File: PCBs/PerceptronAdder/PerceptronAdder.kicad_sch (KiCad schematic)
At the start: 80 parts, among them J1 Conn_02x10, J2 Conn_01x02_Pin, J3 Conn_01x02_Socket, K1 6mm, K10 6mm, K11 6mm, K12 6mm, K13 6mm, K14 6mm, K15 6mm, K16 6mm, K17 6mm, K2 6mm, K3 6mm, K4 6mm, K5 6mm, K6 6mm, K7 6mm, K8 6mm, K9 6mm

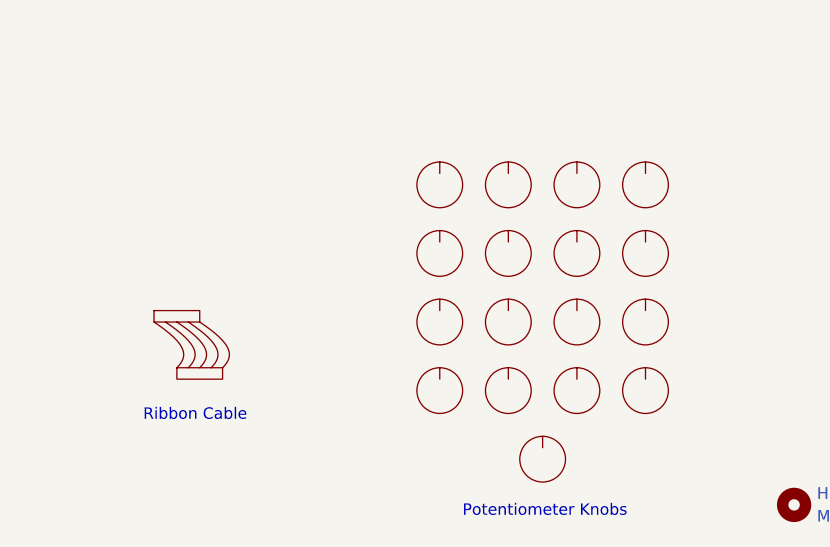
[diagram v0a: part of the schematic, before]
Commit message: Remove knobs from BoM and add alternate link for ribbon cable.
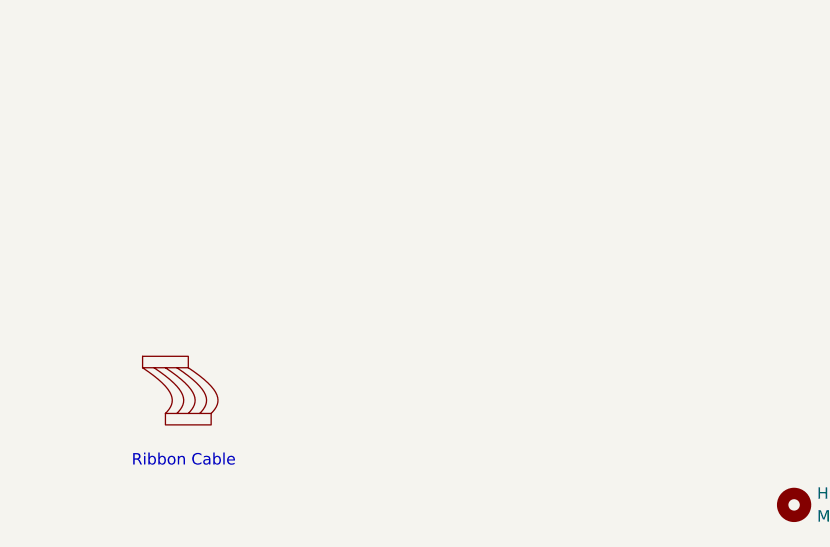
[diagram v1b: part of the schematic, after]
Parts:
- removed K1, K10, K11, K12, K13, K14, K15, K16, K17, K2, K3, K4, K5, K6, K7, K8, K9: 6mm, symbol PerceptronAdderSymbols:Potentiometer_Knob
- RC1: Alt Link (none) -> https://www.digikey.com/en/products/detail/assmann-wsw-comp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
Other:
- note removed: "Potentiometer Knobs"

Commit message: Added resistor values to silkscreen.
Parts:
- R1, R10, R11, R12, R13, R14, R15, R16, R17, R18, R19, R2, R20, R21, R22, R23, R24, R25, R26, R27, R28, R29, R3, R30, R31, R32, R33, R34, R35, R36, R37, R4, R5, R6, R7, R8, R9: footprint Resistor_THT:R_Axial_DIN0207_L6.3mm_D2.5mm_P7.62mm_Horizontal -> PerceptronAdderFootprints:R_Axial_DIN0207_L6.3mm_D2.5mm_P7.62mm_Horizontal
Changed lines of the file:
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@@
 	(title_block
 		(title "Perceptron Adder")
-		(date "2026-03-11")
-		(rev "2.2")
+		(date "2026-05-21")
+		(rev "2.3")
 		(company "RDB64")
 	)
@@
 			)
 		)
-		(property "Footprint" "Resistor_THT:R_Axial_DIN0207_L6.3mm_D2.5mm_P7.62mm_Horizontal"
+		(property "Footprint" "PerceptronAdderFootprints:R_Axial_DIN0207_L6.3mm_D2.5mm_P7.62mm_Horizontal"
 			(at 206.502 83.82 90)
 			(effects
@@
 			)
 		)
-		(property "Footprint" "Resistor_THT:R_Axial_DIN0207_L6.3mm_D2.5mm_P7.62mm_Horizontal"
+		(property "Footprint" "PerceptronAdderFootprints:R_Axial_DIN0207_L6.3mm_D2.5mm_P7.62mm_Horizontal"
 			(at 51.562 83.82 90)
 			(effects
@@
 			)
 		)
-		(property "Footprint" "Resistor_THT:R_Axial_DIN0207_L6.3mm_D2.5mm_P7.62mm_Horizontal"
+		(property "Footprint" "PerceptronAdderFootprints:R_Axial_DIN0207_L6.3mm_D2.5mm_P7.62mm_Horizontal"
 			(at 89.662 83.82 90)
 			(effects
@@
 			)
 		)
-		(property "Footprint" "Resistor_THT:R_Axial_DIN0207_L6.3mm_D2.5mm_P7.62mm_Horizontal"
+		(property "Footprint" "PerceptronAdderFootprints:R_Axial_DIN0207_L6.3mm_D2.5mm_P7.62mm_Horizontal"
 			(at 229.362 83.82 90)
 			(effects
@@
 			)
 		)
-		(property "Footprint" "Resistor_THT:R_Axial_DIN0207_L6.3mm_D2.5mm_P7.62mm_Horizontal"
+		(property "Footprint" "PerceptronAdderFootprints:R_Axial_DIN0207_L6.3mm_D2.5mm_P7.62mm_Horizontal"
 			(at 36.322 83.82 90)
 			(effects
@@
 			)
 		)
-		(property "Footprint" "Resistor_THT:R_Axial_DIN0207_L6.3mm_D2.5mm_P7.62mm_Horizontal"
+		(property "Footprint" "PerceptronAdderFootprints:R_Axial_DIN0207_L6.3mm_D2.5mm_P7.62mm_Horizontal"
 			(at 244.602 83.82 90)
 			(effects
@@
 			)
 		)
-		(property "Footprint" "Resistor_THT:R_Axial_DIN0207_L6.3mm_D2.5mm_P7.62mm_Horizontal"
+		(property "Footprint" "PerceptronAdderFootprints:R_Axial_DIN0207_L6.3mm_D2.5mm_P7.62mm_Horizontal"
 			(at 198.882 83.82 90)
 			(effects
@@
 			)
 		)
-		(property "Footprint" "Resistor_THT:R_Axial_DIN0207_L6.3mm_D2.5mm_P7.62mm_Horizontal"
+		(property "Footprint" "PerceptronAdderFootprints:R_Axial_DIN0207_L6.3mm_D2.5mm_P7.62mm_Horizontal"
 			(at 13.462 83.82 90)
 			(effects
@@
 			)
 		)
-		(property "Footprint" "Resistor_THT:R_Axial_DIN0207_L6.3mm_D2.5mm_P7.62mm_Horizontal"
+		(property "Footprint" "PerceptronAdderFootprints:R_Axial_DIN0207_L6.3mm_D2.5mm_P7.62mm_Horizontal"
 			(at 43.942 83.82 90)
 			(effects
@@
 			)
 		)
-		(property "Footprint" "Resistor_THT:R_Axial_DIN0207_L6.3mm_D2.5mm_P7.62mm_Horizontal"
+		(property "Footprint" "PerceptronAdderFootprints:R_Axial_DIN0207_L6.3mm_D2.5mm_P7.62mm_Horizontal"
 			(at 262.382 83.82 90)
 			(effects
@@
 			)
 		)
-		(property "Footprint" "Resistor_THT:R_Axial_DIN0207_L6.3mm_D2.5mm_P7.62mm_Horizontal"
+		(property "Footprint" "PerceptronAdderFootprints:R_Axial_DIN0207_L6.3mm_D2.5mm_P7.62mm_Horizontal"
 			(at 21.082 83.82 90)
 			(effects
@@
 			)
 		)
-		(property "Footprint" "Resistor_THT:R_Axial_DIN0207_L6.3mm_D2.5mm_P7.62mm_Horizontal"
+		(property "Footprint" "PerceptronAdderFootprints:R_Axial_DIN0207_L6.3mm_D2.5mm_P7.62mm_Horizontal"
 			(at 74.422 83.82 90)
 			(effects
@@
 			)
 		)
-		(property "Footprint" "Resistor_THT:R_Axial_DIN0207_L6.3mm_D2.5mm_P7.62mm_Horizontal"
+		(property "Footprint" "PerceptronAdderFootprints:R_Axial_DIN0207_L6.3mm_D2.5mm_P7.62mm_Horizontal"
 			(at 97.282 83.82 90)
 			(effects
@@
 			)
 		)
-		(property "Footprint" "Resistor_THT:R_Axial_DIN0207_L6.3mm_D2.5mm_P7.62mm_Horizontal"
+		(property "Footprint" "PerceptronAdderFootprints:R_Axial_DIN0207_L6.3mm_D2.5mm_P7.62mm_Horizontal"
 			(at 160.782 83.82 90)
 			(effects
@@
 			)
 		)
-		(property "Footprint" "Resistor_THT:R_Axial_DIN0207_L6.3mm_D2.5mm_P7.62mm_Horizontal"
+		(property "Footprint" "PerceptronAdderFootprints:R_Axial_DIN0207_L6.3mm_D2.5mm_P7.62mm_Horizontal"
 			(at 28.702 83.82 90)
 			(effects
@@
 			)
 		)
-		(property "Footprint" "Resistor_THT:R_Axial_DIN0207_L6.3mm_D2.5mm_P7.62mm_Horizontal"
+		(property "Footprint" "PerceptronAdderFootprints:R_Axial_DIN0207_L6.3mm_D2.5mm_P7.62mm_Horizontal"
 			(at 191.262 83.82 90)
 			(effects
@@
 			)
 		)
-		(property "Footprint" "Resistor_THT:R_Axial_DIN0207_L6.3mm_D2.5mm_P7.62mm_Horizontal"
+		(property "Footprint" "PerceptronAdderFootprints:R_Axial_DIN0207_L6.3mm_D2.5mm_P7.62mm_Horizontal"
 			(at 259.842 114.3 90)
 			(effects
@@
 			)
 		)
-		(property "Footprint" "Resistor_THT:R_Axial_DIN0207_L6.3mm_D2.5mm_P7.62mm_Horizontal"
+		(property "Footprint" "PerceptronAdderFootprints:R_Axial_DIN0207_L6.3mm_D2.5mm_P7.62mm_Horizontal"
 			(at 214.122 83.82 90)
 			(effects
@@
 			)
 		)
-		(property "Footprint" "Resistor_THT:R_Axial_DIN0207_L6.3mm_D2.5mm_P7.62mm_Horizontal"
+		(property "Footprint" "PerceptronAdderFootprints:R_Axial_DIN0207_L6.3mm_D2.5mm_P7.62mm_Horizontal"
 			(at 112.522 83.82 90)
 			(effects
@@
 			)
 		)
-		(property "Footprint" "Resistor_THT:R_Axial_DIN0207_L6.3mm_D2.5mm_P7.62mm_Horizontal"
+		(property "Footprint" "PerceptronAdderFootprints:R_Axial_DIN0207_L6.3mm_D2.5mm_P7.62mm_Horizontal"
 			(at 127.762 83.82 90)
 			(effects
@@
 			)
 		)
-		(property "Footprint" "Resistor_THT:R_Axial_DIN0207_L6.3mm_D2.5mm_P7.62mm_Horizontal"
+		(property "Footprint" "PerceptronAdderFootprints:R_Axial_DIN0207_L6.3mm_D2.5mm_P7.62mm_Horizontal"
 			(at 59.182 83.82 90)
 			(effects
@@
 			)
 		)
-		(property "Footprint" "Resistor_THT:R_Axial_DIN0207_L6.3mm_D2.5mm_P7.62mm_Horizontal"
+		(property "Footprint" "PerceptronAdderFootprints:R_Axial_DIN0207_L6.3mm_D2.5mm_P7.62mm_Horizontal"
 			(at 183.642 83.82 90)
 			(effects
@@
 			)
 		)
-		(property "Footprint" "Resistor_THT:R_Axial_DIN0207_L6.3mm_D2.5mm_P7.62mm_Horizontal"
+		(property "Footprint" "PerceptronAdderFootprints:R_Axial_DIN0207_L6.3mm_D2.5mm_P7.62mm_Horizontal"
 			(at 221.742 83.82 90)
 			(effects
@@
 			)
 		)
-		(property "Footprint" "Resistor_THT:R_Axial_DIN0207_L6.3mm_D2.5mm_P7.62mm_Horizontal"
+		(property "Footprint" "PerceptronAdderFootprints:R_Axial_DIN0207_L6.3mm_D2.5mm_P7.62mm_Horizontal"
 			(at 104.902 83.82 90)
 			(effects
@@
 			)
 		)
-		(property "Footprint" "Resistor_THT:R_Axial_DIN0207_L6.3mm_D2.5mm_P7.62mm_Horizontal"
+		(property "Footprint" "PerceptronAdderFootprints:R_Axial_DIN0207_L6.3mm_D2.5mm_P7.62mm_Horizontal"
 			(at 267.462 114.3 90)
 			(effects
@@
 			)
 		)
-		(property "Footprint" "Resistor_THT:R_Axial_DIN0207_L6.3mm_D2.5mm_P7.62mm_Horizontal"
+		(property "Footprint" "PerceptronAdderFootprints:R_Axial_DIN0207_L6.3mm_D2.5mm_P7.62mm_Horizontal"
 			(at 236.982 83.82 90)
 			(effects
@@
 			)
 		)
-		(property "Footprint" "Resistor_THT:R_Axial_DIN0207_L6.3mm_D2.5mm_P7.62mm_Horizontal"
+		(property "Footprint" "PerceptronAdderFootprints:R_Axial_DIN0207_L6.3mm_D2.5mm_P7.62mm_Horizontal"
 			(at 145.542 83.82 90)
 			(effects
@@
 			)
 		)
-		(property "Footprint" "Resistor_THT:R_Axial_DIN0207_L6.3mm_D2.5mm_P7.62mm_Horizontal"
+		(property "Footprint" "PerceptronAdderFootprints:R_Axial_DIN0207_L6.3mm_D2.5mm_P7.62mm_Horizontal"
 			(at 82.042 83.82 90)
 			(effects
@@
 			)
 		)
-		(property "Footprint" "Resistor_THT:R_Axial_DIN0207_L6.3mm_D2.5mm_P7.62mm_Horizontal"
+		(property "Footprint" "PerceptronAdderFootprints:R_Axial_DIN0207_L6.3mm_D2.5mm_P7.62mm_Horizontal"
 			(at 138.43 113.792 90)
 			(effects
@@
 			)
 		)
-		(property "Footprint" "Resistor_THT:R_Axial_DIN0207_L6.3mm_D2.5mm_P7.62mm_Horizontal"
+		(property "Footprint" "PerceptronAdderFootprints:R_Axial_DIN0207_L6.3mm_D2.5mm_P7.62mm_Horizontal"
 			(at 137.922 83.82 90)
 			(effects
@@
 			)
 		)
-		(property "Footprint" "Resistor_THT:R_Axial_DIN0207_L6.3mm_D2.5mm_P7.62mm_Horizontal"
+		(property "Footprint" "PerceptronAdderFootprints:R_Axial_DIN0207_L6.3mm_D2.5mm_P7.62mm_Horizontal"
 			(at 168.402 83.82 90)
 			(effects
@@
 			)
 		)
-		(property "Footprint" "Resistor_THT:R_Axial_DIN0207_L6.3mm_D2.5mm_P7.62mm_Horizontal"
+		(property "Footprint" "PerceptronAdderFootprints:R_Axial_DIN0207_L6.3mm_D2.5mm_P7.62mm_Horizontal"
 			(at 270.002 83.82 90)
 			(effects
@@
 			)
 		)
-		(property "Footprint" "Resistor_THT:R_Axial_DIN0207_L6.3mm_D2.5mm_P7.62mm_Horizontal"
+		(property "Footprint" "PerceptronAdderFootprints:R_Axial_DIN0207_L6.3mm_D2.5mm_P7.62mm_Horizontal"
 			(at 252.222 83.82 90)
 			(effects
@@
 			)
 		)
-		(property "Footprint" "Resistor_THT:R_Axial_DIN0207_L6.3mm_D2.5mm_P7.62mm_Horizontal"
+		(property "Footprint" "PerceptronAdderFootprints:R_Axial_DIN0207_L6.3mm_D2.5mm_P7.62mm_Horizontal"
 			(at 66.802 83.82 90)
 			(effects
@@
 			)
 		)
-		(property "Footprint" "Resistor_THT:R_Axial_DIN0207_L6.3mm_D2.5mm_P7.62mm_Horizontal"
+		(property "Footprint" "PerceptronAdderFootprints:R_Axial_DIN0207_L6.3mm_D2.5mm_P7.62mm_Horizontal"
 			(at 176.022 83.82 90)
 			(effects
@@
 			)
 		)
-		(property "Footprint" "Resistor_THT:R_Axial_DIN0207_L6.3mm_D2.5mm_P7.62mm_Horizontal"
+		(property "Footprint" "PerceptronAdderFootprints:R_Axial_DIN0207_L6.3mm_D2.5mm_P7.62mm_Horizontal"
 			(at 120.142 83.82 90)
 			(effects
@@
 			)
 		)
-		(property "Footprint" "Resistor_THT:R_Axial_DIN0207_L6.3mm_D2.5mm_P7.62mm_Horizontal"
+		(property "Footprint" "PerceptronAdderFootprints:R_Axial_DIN0207_L6.3mm_D2.5mm_P7.62mm_Horizontal"
 			(at 153.162 83.82 90)
 			(effects

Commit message: Support flat, D-shaped knobs.
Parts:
- RV1, RV10, RV11, RV12, RV13, RV14, RV15, RV16, RV17, RV2, RV3, RV4, RV5, RV6, RV7, RV8, RV9: Alt Link https://www.digikey.com/en/products/detail/bourns-inc/PTV09A-4225S-B103/3820587 -> https://www.digikey.com/en/products/detail/bourns-inc/PTV09A-4220F-B103/3781150
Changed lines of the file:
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@@
 			)
 		)
-		(property "Alt Link" "https://www.digikey.com/en/products/detail/bourns-inc/PTV09A-4225S-B103/3820587"
+		(property "Alt Link" "https://www.digikey.com/en/products/detail/bourns-inc/PTV09A-4220F-B103/3781150"
 			(at 34.29 71.12 90)
 			(effects
@@
 			)
 		)
-		(property "Alt Link" "https://www.digikey.com/en/products/detail/bourns-inc/PTV09A-4225S-B103/3820587"
+		(property "Alt Link" "https://www.digikey.com/en/products/detail/bourns-inc/PTV09A-4220F-B103/3781150"
 			(at 219.71 71.12 90)
 			(effects
@@
 			)
 		)
-		(property "Alt Link" "https://www.digikey.com/en/products/detail/bourns-inc/PTV09A-4225S-B103/3820587"
+		(property "Alt Link" "https://www.digikey.com/en/products/detail/bourns-inc/PTV09A-4220F-B103/3781150"
 			(at 19.05 71.12 90)
 			(effects
@@
 			)
 		)
-		(property "Alt Link" "https://www.digikey.com/en/products/detail/bourns-inc/PTV09A-4225S-B103/3820587"
+		(property "Alt Link" "https://www.digikey.com/en/products/detail/bourns-inc/PTV09A-4220F-B103/3781150"
 			(at 80.01 71.12 90)
 			(effects
@@
 			)
 		)
-		(property "Alt Link" "https://www.digikey.com/en/products/detail/bourns-inc/PTV09A-4225S-B103/3820587"
+		(property "Alt Link" "https://www.digikey.com/en/products/detail/bourns-inc/PTV09A-4220F-B103/3781150"
 			(at 158.75 71.12 90)
 			(effects
@@
 			)
 		)
-		(property "Alt Link" "https://www.digikey.com/en/products/detail/bourns-inc/PTV09A-4225S-B103/3820587"
+		(property "Alt Link" "https://www.digikey.com/en/products/detail/bourns-inc/PTV09A-4220F-B103/3781150"
 			(at 110.49 71.12 90)
 			(effects
@@
 			)
 		)
-		(property "Alt Link" "https://www.digikey.com/en/products/detail/bourns-inc/PTV09A-4225S-B103/3820587"
+		(property "Alt Link" "https://www.digikey.com/en/products/detail/bourns-inc/PTV09A-4220F-B103/3781150"
 			(at 95.25 71.12 90)
 			(effects
@@
 			)
 		)
-		(property "Alt Link" "https://www.digikey.com/en/products/detail/bourns-inc/PTV09A-4225S-B103/3820587"
+		(property "Alt Link" "https://www.digikey.com/en/products/detail/bourns-inc/PTV09A-4220F-B103/3781150"
 			(at 234.95 71.12 90)
 			(effects
@@
 			)
 		)
-		(property "Alt Link" "https://www.digikey.com/en/products/detail/bourns-inc/PTV09A-4225S-B103/3820587"
+		(property "Alt Link" "https://www.digikey.com/en/products/detail/bourns-inc/PTV09A-4220F-B103/3781150"
 			(at 204.47 71.12 90)
 			(effects
@@
 			)
 		)
-		(property "Alt Link" "https://www.digikey.com/en/products/detail/bourns-inc/PTV09A-4225S-B103/3820587"
+		(property "Alt Link" "https://www.digikey.com/en/products/detail/bourns-inc/PTV09A-4220F-B103/3781150"
 			(at 125.73 71.12 90)
 			(effects
@@
 			)
 		)
-		(property "Alt Link" "https://www.digikey.com/en/products/detail/bourns-inc/PTV09A-4225S-B103/3820587"
+		(property "Alt Link" "https://www.digikey.com/en/products/detail/bourns-inc/PTV09A-4220F-B103/3781150"
 			(at 64.77 71.12 90)
 			(effects
@@
 			)
 		)
-		(property "Alt Link" "https://www.digikey.com/en/products/detail/bourns-inc/PTV09A-4225S-B103/3820587"
+		(property "Alt Link" "https://www.digikey.com/en/products/detail/bourns-inc/PTV09A-4220F-B103/3781150"
 			(at 143.51 71.12 90)
 			(effects
@@
 			)
 		)
-		(property "Alt Link" "https://www.digikey.com/en/products/detail/bourns-inc/PTV09A-4225S-B103/3820587"
+		(property "Alt Link" "https://www.digikey.com/en/products/detail/bourns-inc/PTV09A-4220F-B103/3781150"
 			(at 250.19 71.12 90)
 			(effects
@@
 			)
 		)
-		(property "Alt Link" "https://www.digikey.com/en/products/detail/bourns-inc/PTV09A-4225S-B103/3820587"
+		(property "Alt Link" "https://www.digikey.com/en/products/detail/bourns-inc/PTV09A-4220F-B103/3781150"
 			(at 267.97 71.12 90)
 			(effects
@@
 			)
 		)
-		(property "Alt Link" "https://www.digikey.com/en/products/detail/bourns-inc/PTV09A-4225S-B103/3820587"
+		(property "Alt Link" "https://www.digikey.com/en/products/detail/bourns-inc/PTV09A-4220F-B103/3781150"
 			(at 189.23 71.12 90)
 			(effects
@@
 			)
 		)
-		(property "Alt Link" "https://www.digikey.com/en/products/detail/bourns-inc/PTV09A-4225S-B103/3820587"
+		(property "Alt Link" "https://www.digikey.com/en/products/detail/bourns-inc/PTV09A-4220F-B103/3781150"
 			(at 173.99 71.12 90)
 			(effects
@@
 			)
 		)
-		(property "Alt Link" "https://www.digikey.com/en/products/detail/bourns-inc/PTV09A-4225S-B103/3820587"
+		(property "Alt Link" "https://www.digikey.com/en/products/detail/bourns-inc/PTV09A-4220F-B103/3781150"
 			(at 49.53 71.12 90)
 			(effects
